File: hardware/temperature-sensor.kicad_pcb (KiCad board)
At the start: 2 copper layers, 70 x 60 mm, 37 parts, among them J1 USB_B, J2 Barrel_Jack, J3 Conn_01x02_Pin, J4 Conn_01x03, SW1 SW_Push, U1 MCP2221AxP, U2 MCP1702-3302E, U3 ESP-01v090, U4 AHT10

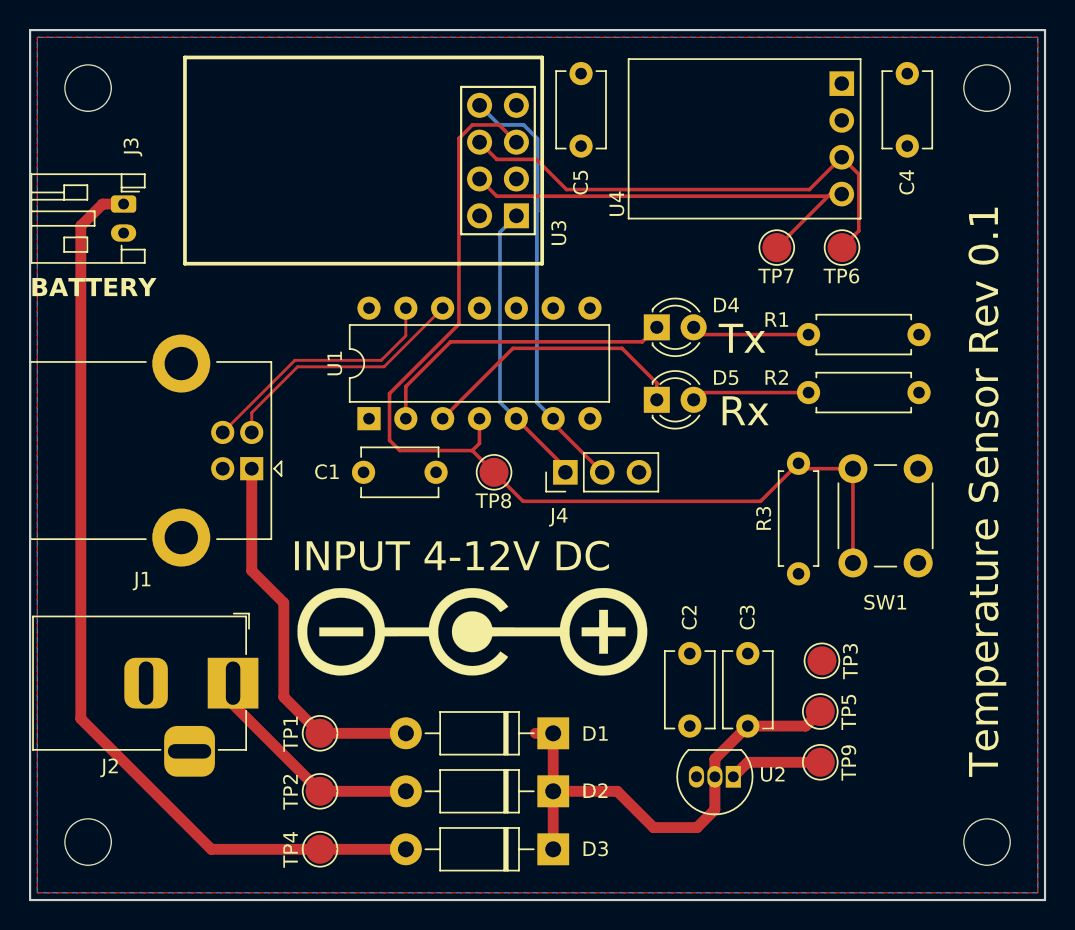
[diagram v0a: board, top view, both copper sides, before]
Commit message: Rev 0.2 - Added jumper to support UART boot
Signed-off-by: Matthew <mnickson@sidingsmedia.com>
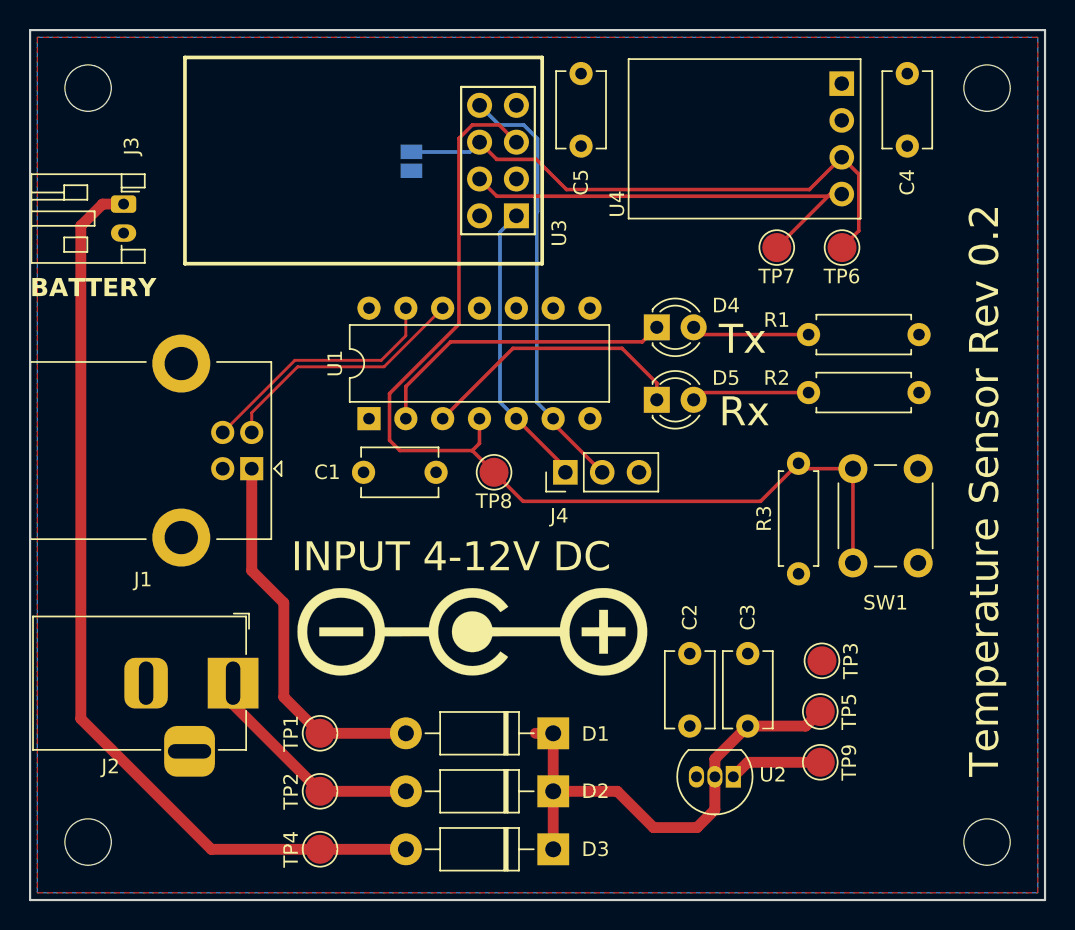
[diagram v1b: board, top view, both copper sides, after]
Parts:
- added JP1: SolderJumper_2_Open, Jumper:SolderJumper-2_P1.3mm_Open_Pad1.0x1.5mm, B.Cu at (136.8, 82.0)
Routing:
- net /TEMP_I2C_SCL: track 34.5 -> 39.4 mm
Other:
- board text added: "Temperature Sensor Rev 0.2"
- board text added: "Temperature Sensor Rev 0.2 Designed by Sidings Media Licenced under CERN-OHL-P-2.0 or any later version www.sidingsmedia.com"
- board text removed: "Temperature Sensor Rev 0.1"
- board text removed: "Temperature Sensor Rev 0.1 Designed by Sidings Media Licenced under CERN-OHL-P-2.0 or any later version www.sidingsmedia.com"
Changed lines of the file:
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@@
   (title_block
     (title "Temperature Sensor")
-    (date "2024-01-07")
-    (rev "0.1")
+    (date "2024-01-13")
+    (rev "0.2")
     (company "Sidings Media")
     (comment 1 "Licence: CERN-OHL-P-2.0 or any later version")
@@
     )
   )
+  (footprint "Jumper:SolderJumper-2_P1.3mm_Open_Pad1.0x1.5mm" (layer "B.Cu")
+    (at 136.8 82.05 -90)
+    (descr "SMD Solder Jumper, 1x1.5mm Pads, 0.3mm gap, open")
+    (tags "solder jumper open")
+    (property "Sheetfile" "temperature-sensor.kicad_sch")
+    (property "Sheetname" "")
+    (property "ki_description" "Solder Jumper, 2-pole, open")
+    (property "ki_keywords" "solder jumper SPST")
+    (attr exclude_from_pos_files)
+    (fp_text reference "JP1" (at 0 1.8 90) (layer "B.SilkS")
+        (effects (font (size 1 1) (thickness 0.15)) (justify mirror))
+    )
+    (fp_text value "SolderJumper_2_Open" (at 0 -1.9 90) (layer "B.Fab")
+        (effects (font (size 1 1) (thickness 0.15)) (justify mirror))
+    )
+    (fp_line (start -1.4 -1) (end -1.4 1)
+      (stroke (width 0.12) (type solid)) (layer "B.SilkS"))
+    (fp_line (start -1.4 1) (end 1.4 1)
+      (stroke (width 0.12) (type solid)) (layer "B.SilkS"))
+    (fp_line (start 1.4 -1) (end -1.4 -1)
+      (stroke (width 0.12) (type solid)) (layer "B.SilkS"))
+    (fp_line (start 1.4 1) (end 1.4 -1)
+      (stroke (width 0.12) (type solid)) (layer "B.SilkS"))
+    (fp_line (start -1.65 1.25) (end -1.65 -1.25)
+      (stroke (width 0.05) (type solid)) (layer "B.CrtYd"))
+    (fp_line (start -1.65 1.25) (end 1.65 1.25)
+      (stroke (width 0.05) (type solid)) (layer "B.CrtYd"))
+    (fp_line (start 1.65 -1.25) (end -1.65 -1.25)
+      (stroke (width 0.05) (type solid)) (layer "B.CrtYd"))
+    (fp_line (start 1.65 -1.25) (end 1.65 1.25)
+      (stroke (width 0.05) (type solid)) (layer "B.CrtYd"))
+    (pad "1" smd rect (at -0.65 0 270) (size 1 1.5) (layers "B.Cu" "B.Mask")
+      (net 14 "/TEMP_I2C_SCL") (pinfunction "A") (pintype "passive"))
+    (pad "2" smd rect (at 0.65 0 270) (size 1 1.5) (layers "B.Cu" "B.Mask")
+      (net 2 "GND") (pinfunction "B") (pintype "passive"))
+  )
   (footprint "Symbol:WEEE-Logo_8.4x12mm_SilkScreen" (layer "B.Cu")
     (at 132 111.5 180)
@@
   (gr_rect (start 110.5 73) (end 180.5 133)
     (stroke (width 0.15) (type default)) (fill none) (layer "Edge.Cuts"))
-  (gr_text "Temperature Sensor Rev 0.1\nDesigned by Sidings Media\nLicenced under CERN-OHL-P-2.0 \nor any later version\nwww.sidingsmedia.com" (at 162 113.5) (layer "B.SilkS")
+  (gr_text "Temperature Sensor Rev 0.2\nDesigned by Sidings Media\nLicenced under CERN-OHL-P-2.0 \nor any later version\nwww.sidingsmedia.com" (at 162 113.5) (layer "B.SilkS")
     (effects (font (size 1 1) (thickness 0.153)) (justify left bottom mirror))
   )
@@
     (effects (font (size 2 2) (thickness 0.3)) (justify left bottom))
   )
-  (gr_text "Temperature Sensor Rev 0.1" (at 177.5 124.5 90) (layer "F.SilkS")
+  (gr_text "Temperature Sensor Rev 0.2" (at 177.5 124.5 90) (layer "F.SilkS")
     (effects (font (size 2 2) (thickness 0.3)) (justify left bottom))
   )
@@
   (segment (start 145.4186 81.9186) (end 147.5 84) (width 0.25) (layer "F.Cu") (net 14))
   (segment (start 167.655 86.845) (end 167.655 82.945) (width 0.25) (layer "F.Cu") (net 14))
+  (segment (start 140.831 81.4) (end 141.501 80.73) (width 0.25) (layer "B.Cu") (net 14))
+  (segment (start 136.8 81.4) (end 140.831 81.4) (width 0.25) (layer "B.Cu") (net 14))
   (segment (start 162 88) (end 165.69 84.31) (width 0.25) (layer "F.Cu") (net 15))
   (segment (start 141.501 83.27) (end 142.6896 84.4586) (width 0.25) (layer "F.Cu") (net 15))

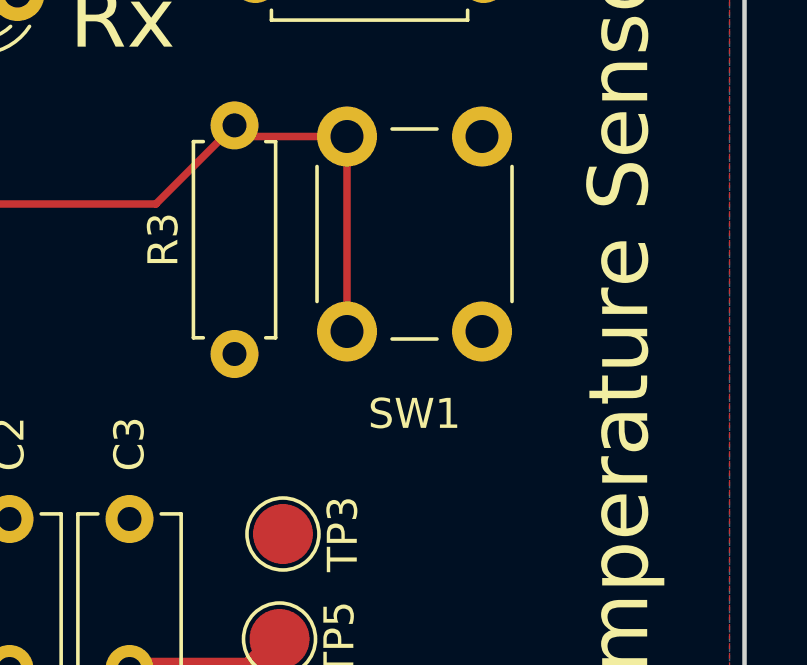
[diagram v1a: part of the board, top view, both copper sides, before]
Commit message: Fixed fab references
Signed-off-by: Matthew <mnickson@sidingsmedia.com>
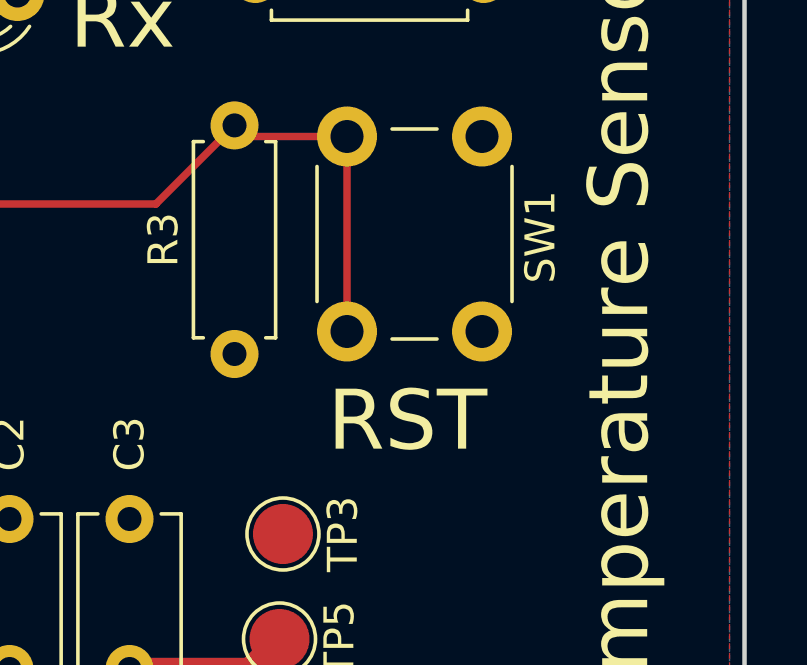
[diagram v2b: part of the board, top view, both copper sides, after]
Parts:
- J3: value Conn_01x02_Pin -> JST S2B-PH-K-S
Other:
- board text added: "RST"

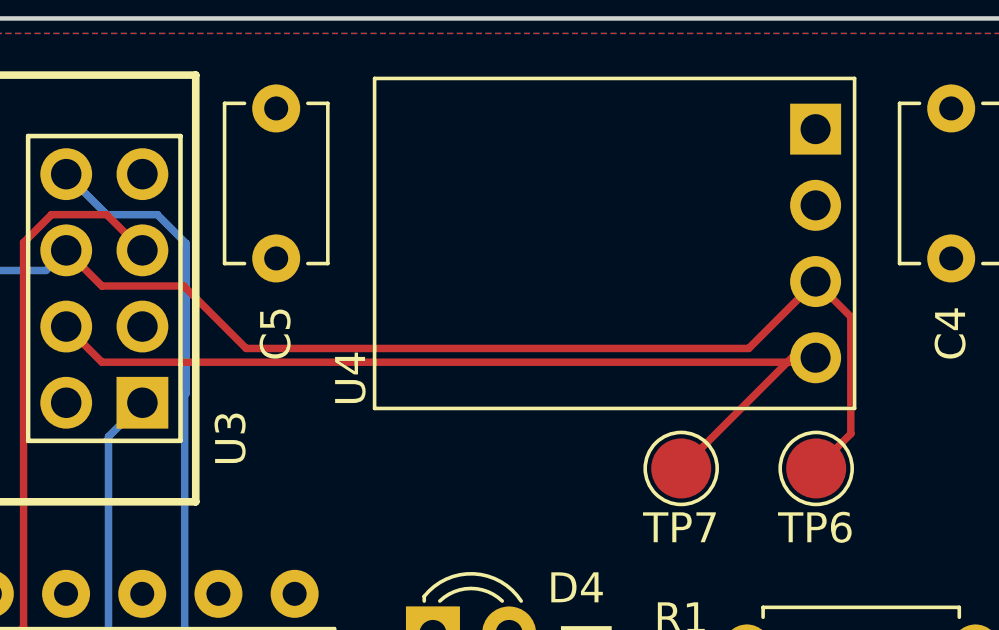
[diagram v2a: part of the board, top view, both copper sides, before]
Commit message: Separated I2C tracks
Signed-off-by: Matthew <mnickson@sidingsmedia.com>
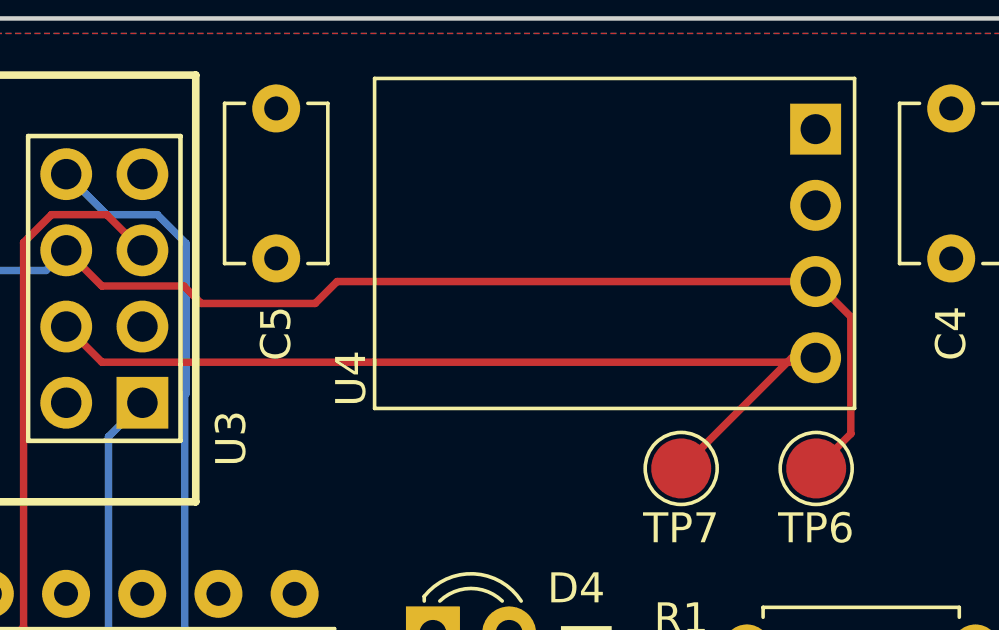
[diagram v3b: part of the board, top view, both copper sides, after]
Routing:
- net /TEMP_I2C_SCL: track 39.4 -> 38.2 mm
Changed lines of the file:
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@@
   (segment (start 141 102) (end 142.5 103.5) (width 0.25) (layer "F.Cu") (net 13))
   (segment (start 141 102) (end 141.495 101.505) (width 0.25) (layer "F.Cu") (net 13))
+  (segment (start 145.4186 81.9186) (end 146 82.5) (width 0.25) (layer "F.Cu") (net 14))
   (segment (start 167.655 82.945) (end 166.48 81.77) (width 0.25) (layer "F.Cu") (net 14))
   (segment (start 166.5 88) (end 167.655 86.845) (width 0.25) (layer "F.Cu") (net 14))
-  (segment (start 164.25 84) (end 166.48 81.77) (width 0.25) (layer "F.Cu") (net 14))
+  (segment (start 149.8 82.5) (end 150.53 81.77) (width 0.25) (layer "F.Cu") (net 14))
   (segment (start 142.6896 81.9186) (end 145.4186 81.9186) (width 0.25) (layer "F.Cu") (net 14))
   (segment (start 141.501 80.73) (end 142.6896 81.9186) (width 0.25) (layer "F.Cu") (net 14))
-  (segment (start 147.5 84) (end 164.25 84) (width 0.25) (layer "F.Cu") (net 14))
-  (segment (start 145.4186 81.9186) (end 147.5 84) (width 0.25) (layer "F.Cu") (net 14))
+  (segment (start 146 82.5) (end 149.8 82.5) (width 0.25) (layer "F.Cu") (net 14))
+  (segment (start 150.53 81.77) (end 166.48 81.77) (width 0.25) (layer "F.Cu") (net 14))
   (segment (start 167.655 86.845) (end 167.655 82.945) (width 0.25) (layer "F.Cu") (net 14))
   (segment (start 140.831 81.4) (end 141.501 80.73) (width 0.25) (layer "B.Cu") (net 14))
